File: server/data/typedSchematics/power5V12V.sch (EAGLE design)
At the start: 3 parts, among them J1 DCJ0202

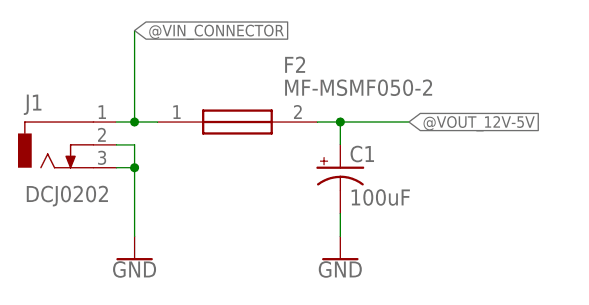
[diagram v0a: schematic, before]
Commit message: Fix voltage ranges
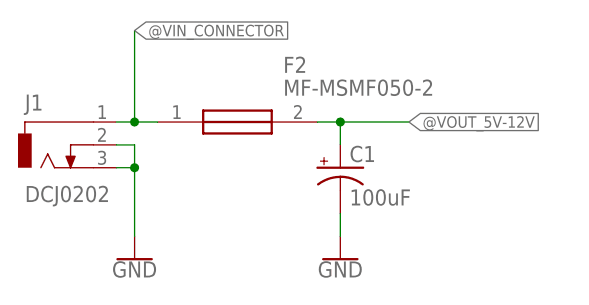
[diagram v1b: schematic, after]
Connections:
- net @VOUT_12V-5V renamed @VOUT_5V-12V
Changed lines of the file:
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@@
 </segment>
 </net>
-<net name="@VOUT_12V-5V" class="0">
+<net name="@VOUT_5V-12V" class="0">
 <segment>
 <wire x1="48.26" y1="27.94" x2="40.64" y2="27.94" width="0.1524" layer="91"/>

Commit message: Remove VIN for power connector
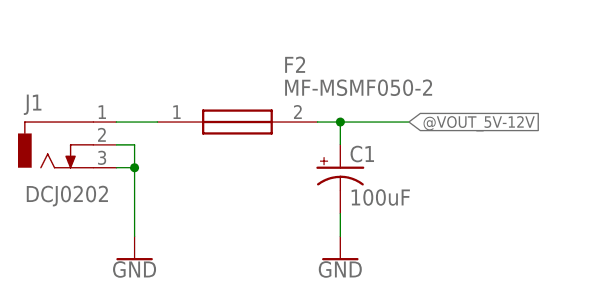
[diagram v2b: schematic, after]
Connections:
- net @VIN_CONNECTOR renamed N$1
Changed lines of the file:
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@@
-</segment>
-</net>
-<net name="@VIN_CONNECTOR" class="0">
-<segment>
-<pinref part="J1" gate="G$1" pin="1"/>
-<pinref part="F2" gate="G$1" pin="1"/>
-<wire x1="15.748" y1="27.94" x2="17.78" y2="27.94" width="0.1524" layer="91"/>
-<wire x1="17.78" y1="27.94" x2="20.32" y2="27.94" width="0.1524" layer="91"/>
-<wire x1="17.78" y1="27.94" x2="17.78" y2="38.1" width="0.1524" layer="91"/>
-<junction x="17.78" y="27.94"/>
-<label x="17.78" y="38.1" size="1.27" layer="95" xref="yes"/>
 </segment>
 </net>
@@
 </segment>
 </net>
+<net name="N$1" class="0">
+<segment>
+<pinref part="J1" gate="G$1" pin="1"/>
+<pinref part="F2" gate="G$1" pin="1"/>
+<wire x1="15.748" y1="27.94" x2="20.32" y2="27.94" width="0.1524" layer="91"/>
+</segment>
+</net>
